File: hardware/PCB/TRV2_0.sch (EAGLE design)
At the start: 56 parts, among them IC1 TMP112, IC2 SHT21, IC4 CNY70, IC5 ATMEGA8-AU, Q1 FC-12M, U1 DRV8850_RGY_24

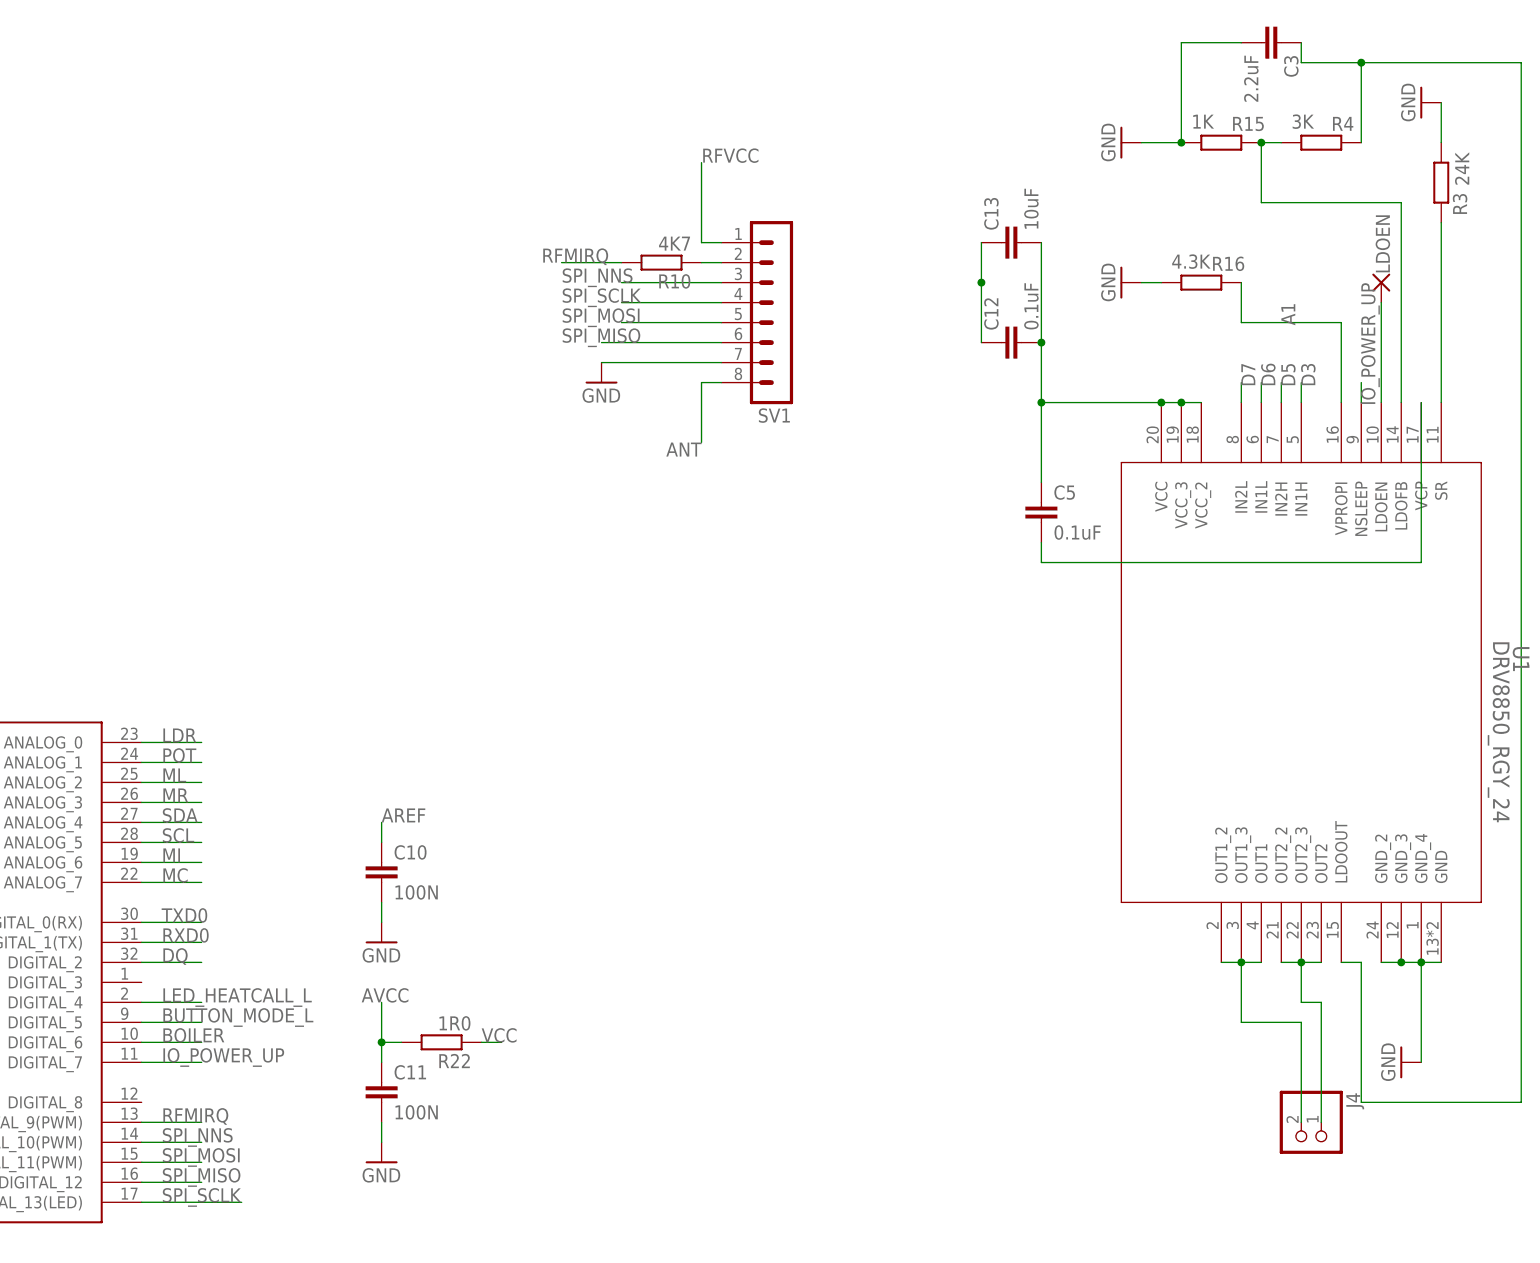
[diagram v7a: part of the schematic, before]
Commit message: png's updated and motordriver placed on board
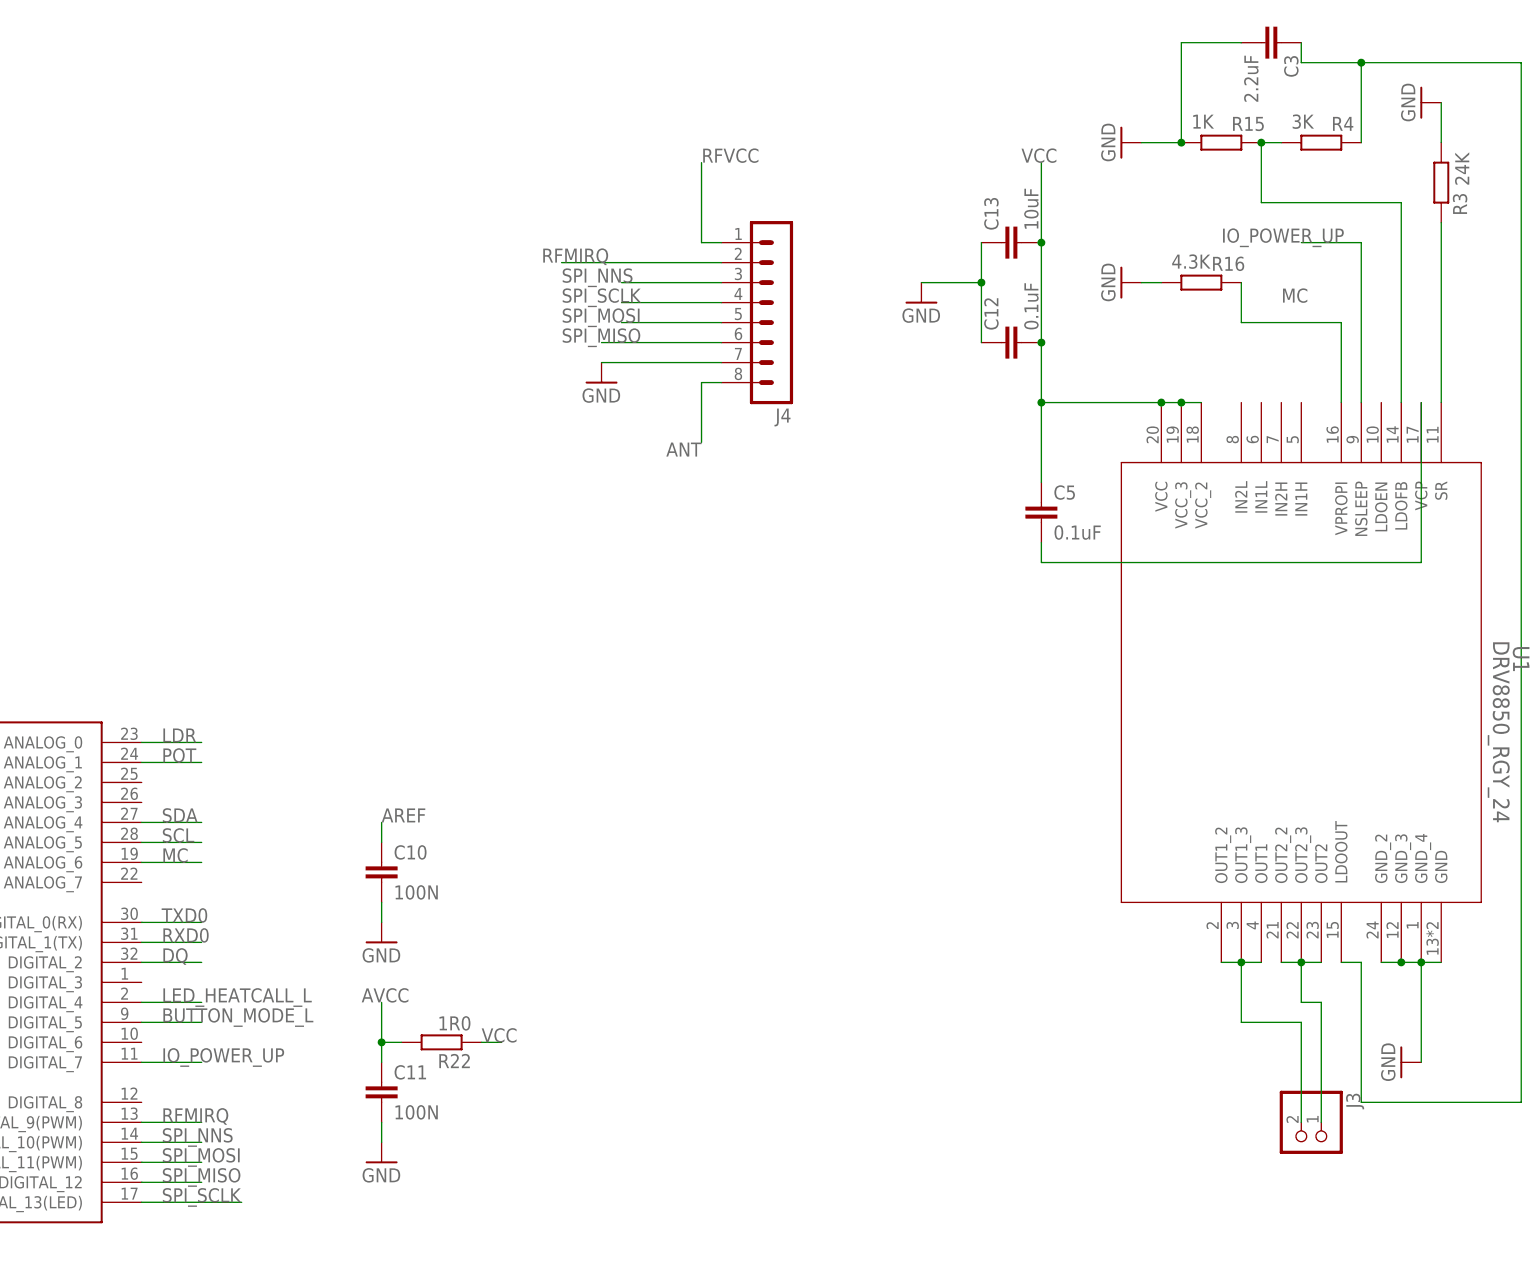
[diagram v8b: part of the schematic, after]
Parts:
- removed LDOEN: WIREPAD2,15/1,0, wirepad:WIREPAD2,15/1,0
- removed R10: 4K7, resistor:R-EU_R0603
- removed SV1: (no value), con-lstb:MA08-1
- added J3: (no value), pinhead:PINHD-1X2
- J4: device pinhead:PINHD-1X2 -> con-lstb:MA08-1
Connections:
- removed net A1: R16.2, U1.VPROPI
- removed net BOILER: IC5.DIGITAL_6
- removed net D3: U1.IN1H
- removed net D5: U1.IN2H
- removed net D6: U1.IN1L
- removed net D7: U1.IN2L
- removed net ML: IC5.ANALOG_2
- removed net MR: IC5.ANALOG_3
- removed net N$16: LDOEN.P, U1.LDOEN
- removed net N$3: R10.1, SV1.2
- removed net VCC1: C12.2, C13.2, C5.1, U1.VCC, U1.VCC_2, U1.VCC_3
- net ANT: now also J4.8; no longer SV1.8
- net GND: now also J4.7; no longer SV1.7
- net MC: now also IC5.ANALOG_6, R16.2, U1.VPROPI; no longer IC5.ANALOG_7
- net MI: no longer IC5.ANALOG_6
- net N$11: now also J3.1; no longer J4.1
- net N$2: now also J3.2; no longer J4.2
- net RFMIRQ: now also J4.2; no longer R10.2
- net RFVCC: now also J4.1; no longer SV1.1
- net SPI_MISO: now also J4.6; no longer SV1.6
- net SPI_MOSI: now also J4.5; no longer SV1.5
- net SPI_NNS: now also J4.3; no longer SV1.3
- net SPI_SCLK: now also J4.4; no longer SV1.4
- net VCC: now also C12.2, C13.2, C5.1, U1.VCC, U1.VCC_2, U1.VCC_3
